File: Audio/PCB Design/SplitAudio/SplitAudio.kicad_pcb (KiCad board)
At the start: 2 copper layers, 113.1 x 113.1 mm, 6 parts, among them J1 AudioJack3, J2 AudioJack3, SW1 SW_Push, SW2 SW_Push, U1 DFPLAYER_MINI

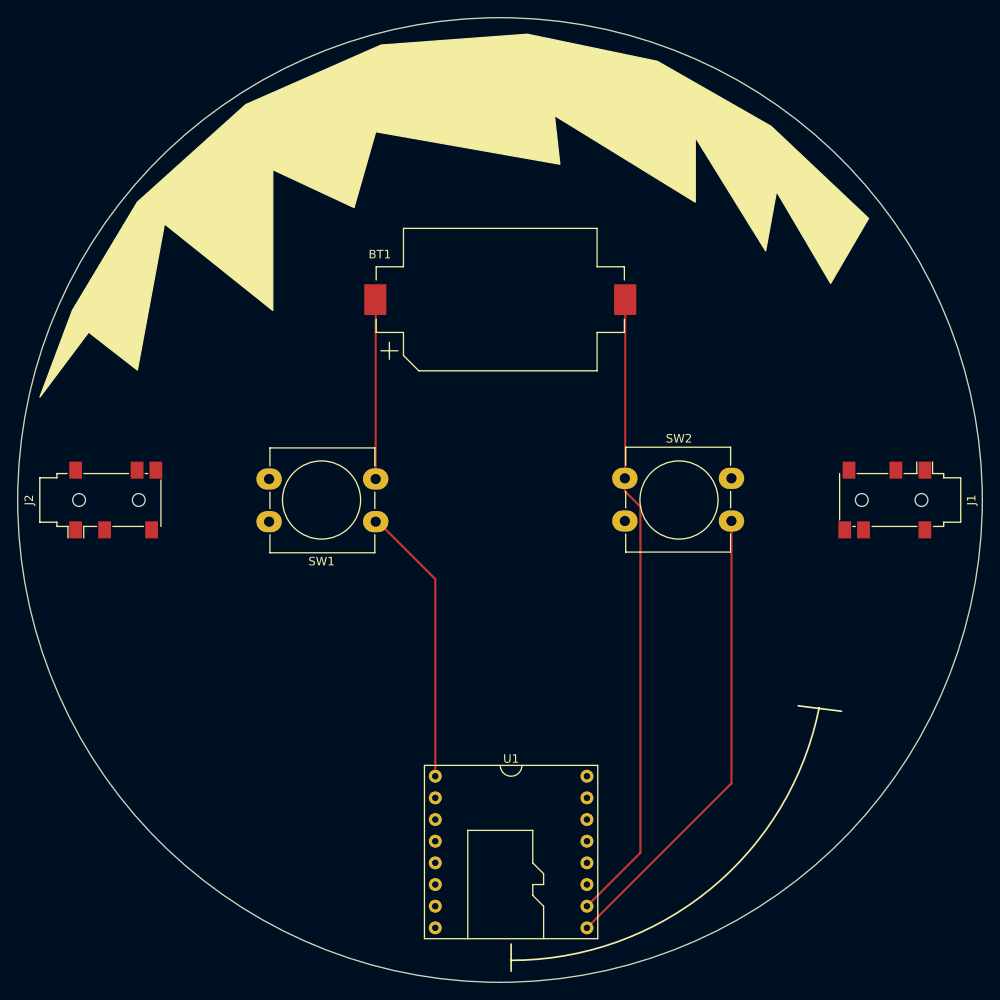
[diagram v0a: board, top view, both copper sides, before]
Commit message: Audio board completed
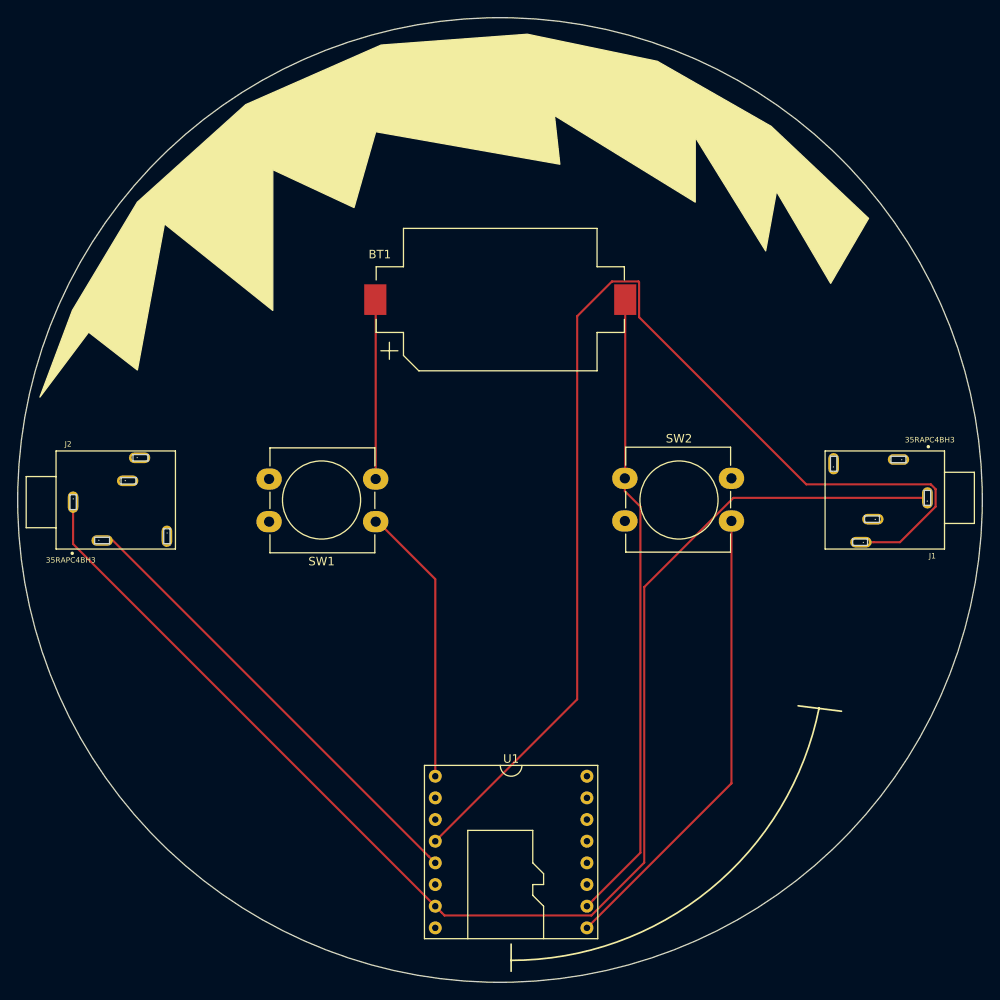
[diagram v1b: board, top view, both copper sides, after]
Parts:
- J1, J2: value AudioJack3 -> 35RAPC4BH3; footprint Connector_Audio:Jack_3.5mm_PJ311_Horizontal -> AudioJack:SWITCHCRAFT_35RAPC4BH3
- turned J1 to 180 degrees
- turned J2 to 0 degrees
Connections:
- J1 pad 1: (no net) -> Net-(J1-Pad1)
- J1 pad 2: (no net) -> Net-(J1-Pad2)
- J1 pad 3: (no net) -> Net-(J1-Pad3)
- J1 pad 4: (no net) -> Net-(J1-Pad4)
- J1 pad 5: (no net) -> Net-(J1-Pad5)
- J2 pad 1: (no net) -> Net-(J1-Pad1)
- J2 pad 2: (no net) -> Net-(J2-Pad2)
- J2 pad 3: (no net) -> Net-(J2-Pad3)
- J2 pad 4: (no net) -> Net-(J2-Pad4)
- J2 pad 5: (no net) -> Net-(J2-Pad5)
- U1 pad 4: Net-(J1-PadR) -> Net-(J1-Pad2)
- U1 pad 5: Net-(J2-PadT) -> Net-(J2-Pad5)
- U1 pad 7: Net-(J1-PadS) -> Net-(J1-Pad1)
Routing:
- net Net-(J1-Pad1): track 0.00 -> 162.3 mm
- net Net-(J1-Pad2): track 0.00 -> 137.2 mm
- net Net-(J2-Pad5): track 0.00 -> 54.7 mm
